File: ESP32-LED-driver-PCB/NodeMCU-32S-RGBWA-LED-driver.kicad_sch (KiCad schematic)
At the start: 24 parts, among them J1 PJ-037A, J2 TBP02R1-381-05BE, Q1 AO6404, Q2 AO6404, Q3 AO6404, Q4 AO6404, U1 NodeMCU-32S, U2 NCP1117-3.3_SOT223

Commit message: Re-organising folders
Re-organising folders
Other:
- note added: "5V to 12V, 5A input current maximum"
- note added: "For driving addressable LEDs: Remove resistors from R1-R4 and place them on R5-R7 Bridge JP1-JP3"
- note removed: "5V to 12V, 5A input power maximum"
- note removed: "For driving addressable LEDs: Remove resistors from R1-R4 and place them on R5-R7 Bridge JP1-JP3 Place 0R resistors R5-R7"
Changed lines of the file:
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@@
     (stroke (width 0) (type default) (color 0 0 0 0))
   )
-  (text "For driving addressable LEDs:\nRemove resistors from R1-R4 and place them on R5-R7\nBridge JP1-JP3\nPlace 0R resistors R5-R7\n"
+  (text "For driving addressable LEDs:\nRemove resistors from R1-R4 and place them on R5-R7\nBridge JP1-JP3"
     (at 137.16 52.07 0)
     (effects (font (size 1.27 1.27)) (justify left bottom))
   )
-  (text "5V to 12V, 5A input power maximum" (at 52.07 151.13 0)
+  (text "5V to 12V, 5A input current maximum" (at 52.07 151.13 0)
     (effects (font (size 1.27 1.27)) (justify left bottom))
   )

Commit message: Updated silkscreen
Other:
- note added: "For driving addressable LEDs: Remove 0R resistors from R1-R4 Place 0R resistors on R5-R7 Bridge JP1-JP3"
- note removed: "For driving addressable LEDs: Remove resistors from R1-R4 and place them on R5-R7 Bridge JP1-JP3"
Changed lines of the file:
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@@
     (stroke (width 0) (type default) (color 0 0 0 0))
   )
-  (text "For driving addressable LEDs:\nRemove resistors from R1-R4 and place them on R5-R7\nBridge JP1-JP3"
+  (text "For driving addressable LEDs:\nRemove 0R resistors from R1-R4\nPlace 0R resistors on R5-R7\nBridge JP1-JP3"
     (at 137.16 52.07 0)
     (effects (font (size 1.27 1.27)) (justify left bottom))

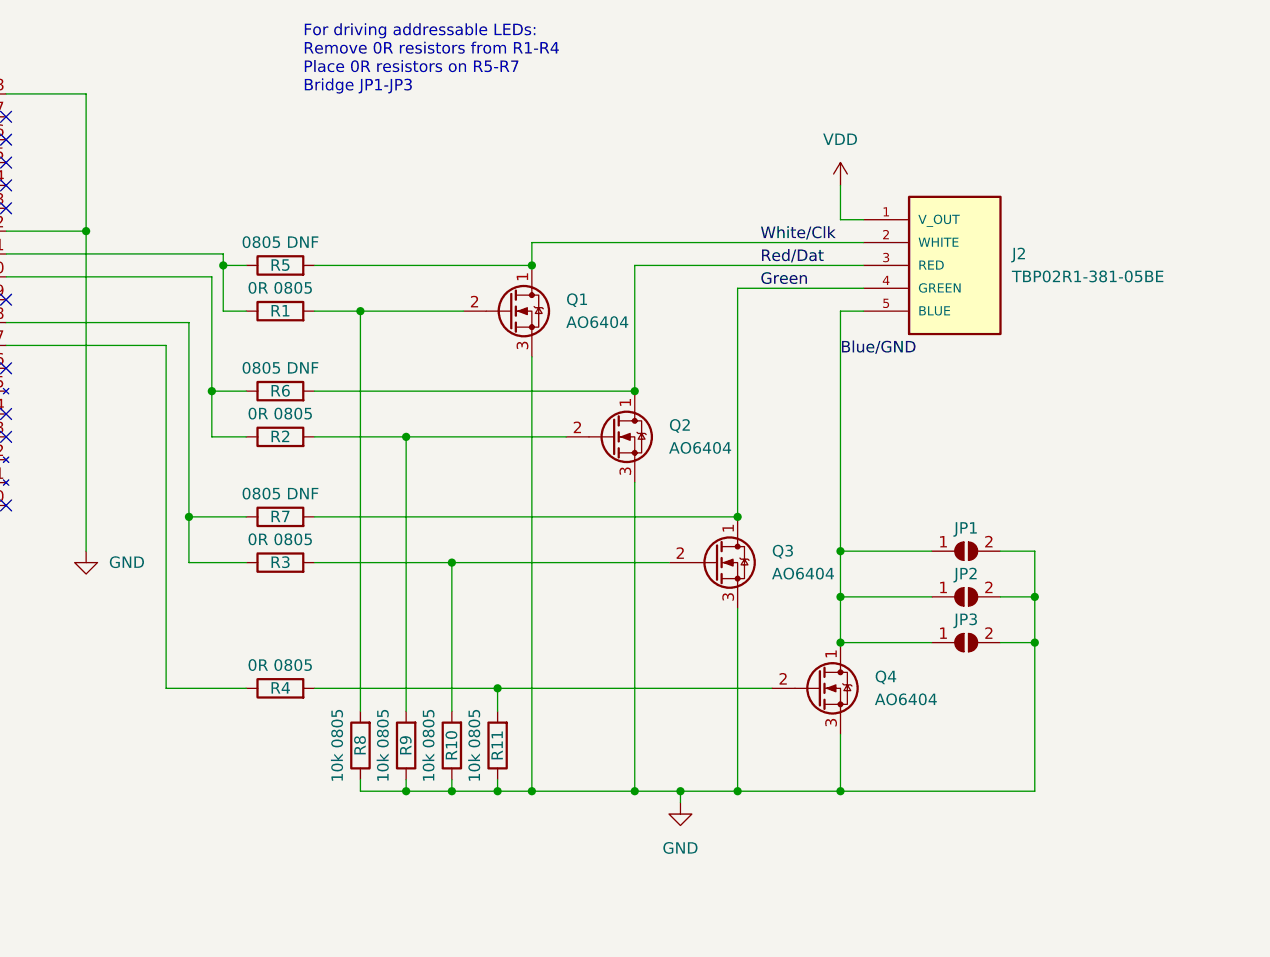
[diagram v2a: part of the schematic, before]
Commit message: Updated to 6 pin connector
Moved to 6 pin connector to get more addressable outputs with a dedicated ground pin.
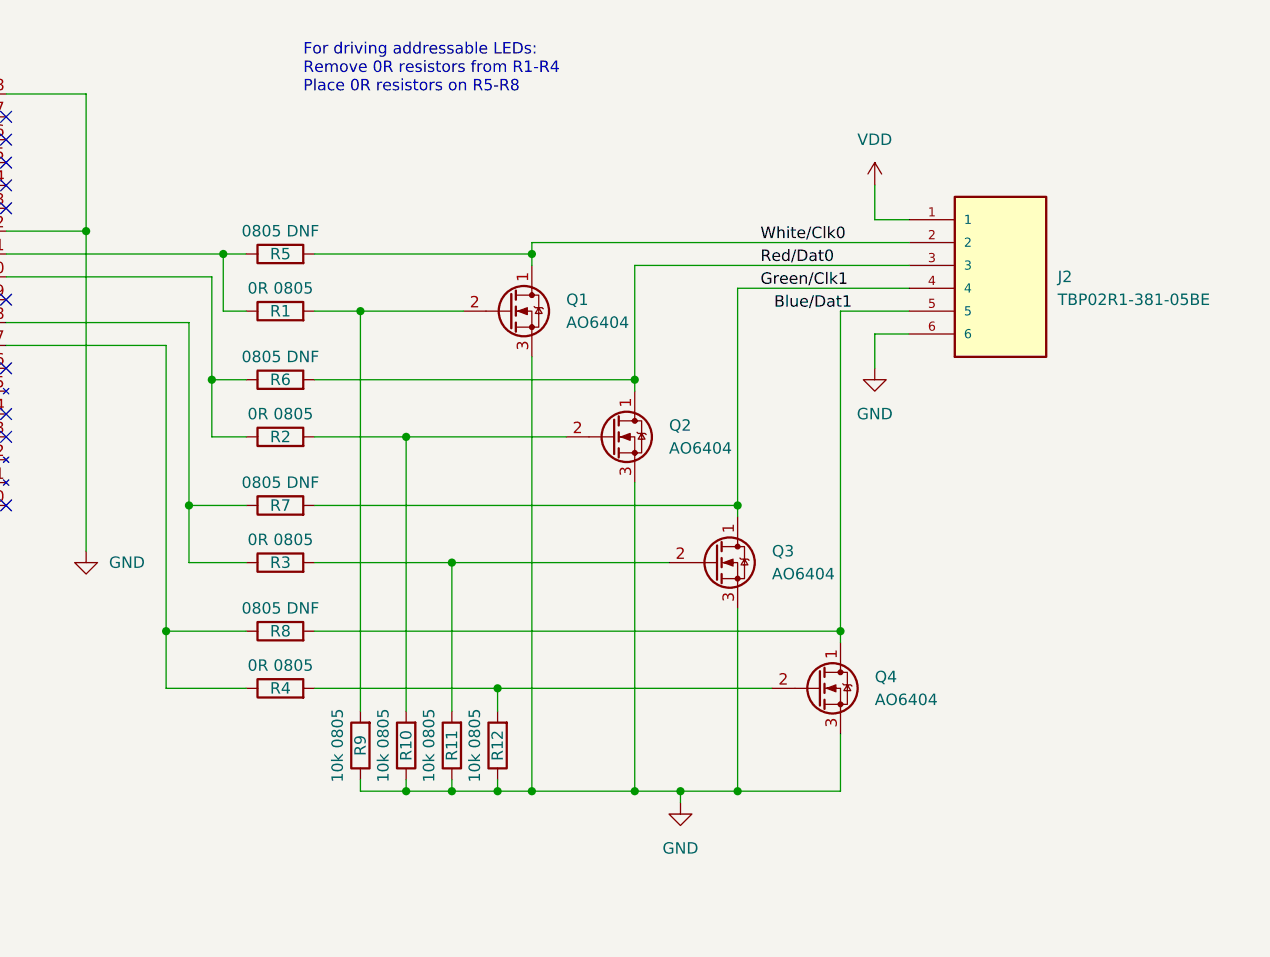
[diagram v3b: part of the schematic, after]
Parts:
- removed J2: TBP02R1-381-05BE, Matts_Library:CUI_TBP02R1-381-05BE, symbol Matts_Library:TBP02R1-381-05BE
- removed JP1, JP2, JP3: SolderJumper_2_Open, Jumper:SolderJumper-2_P1.3mm_Open_TrianglePad1.0x1.5mm, symbol Jumper:SolderJumper_2_Open
- added J2: TBP02R1-381-05BE, Matts_Library:CUI_TBP02R1-381-06BE, symbol Matts_Library:TBP02R1-381-06BE
- added R8: 0805 DNF, Resistor_SMD:R_0805_2012Metric, symbol Device:R
- renumbered R9 to R10, R10 to R11, R11 to R12, R8 to R9
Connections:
- net GND: now also J2.6
- net VDD: now also J2.1
- net at R4.1, U1.27 (IO16): now also R8.1
- net Blue/GND renamed Blue/Dat1
- net Blue/Dat1: now also J2.5, R8.2
- net Green renamed Green/Clk1
- net Green/Clk1: now also J2.4
- net Red/Dat renamed Red/Dat0
- net Red/Dat0: now also J2.3
- net White/Clk renamed White/Clk0
- net White/Clk0: now also J2.2
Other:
- note added: "For driving addressable LEDs: Remove 0R resistors from R1-R4 Place 0R resistors on R5-R8"
- note removed: "For driving addressable LEDs: Remove 0R resistors from R1-R4 Place 0R resistors on R5-R7 Bridge JP1-JP3"
- moved on the sheet: R5, R6, R7

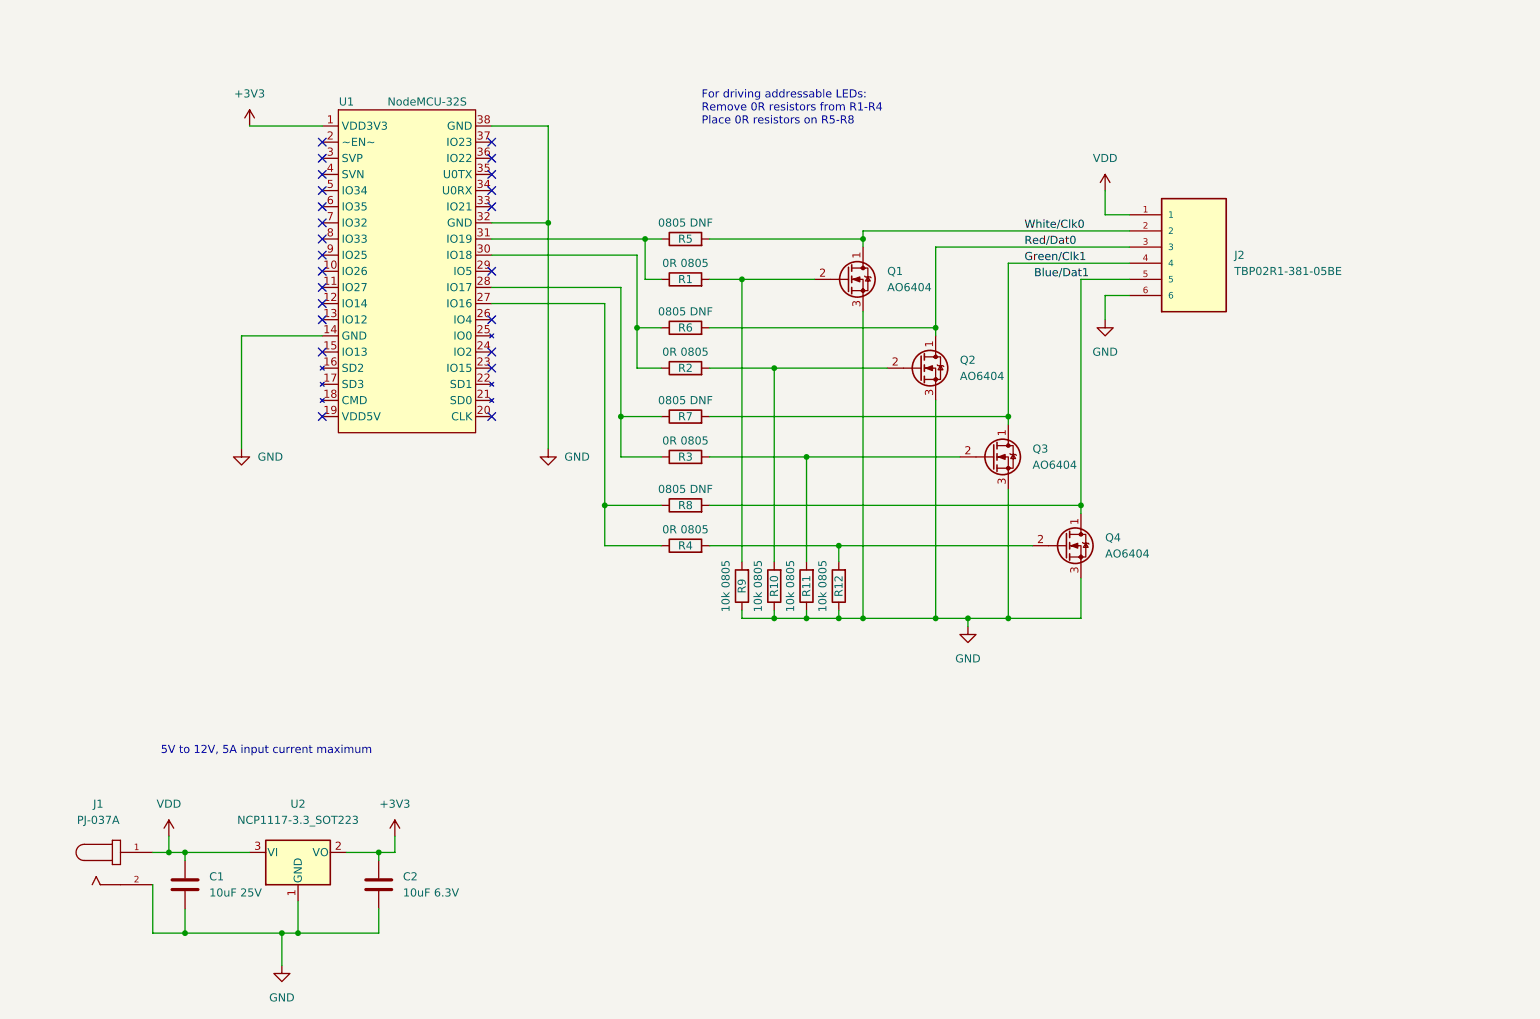
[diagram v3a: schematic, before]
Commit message: Added prototyping area
Added prototyping area to allow for extra sensors.
Updated some silkscreen
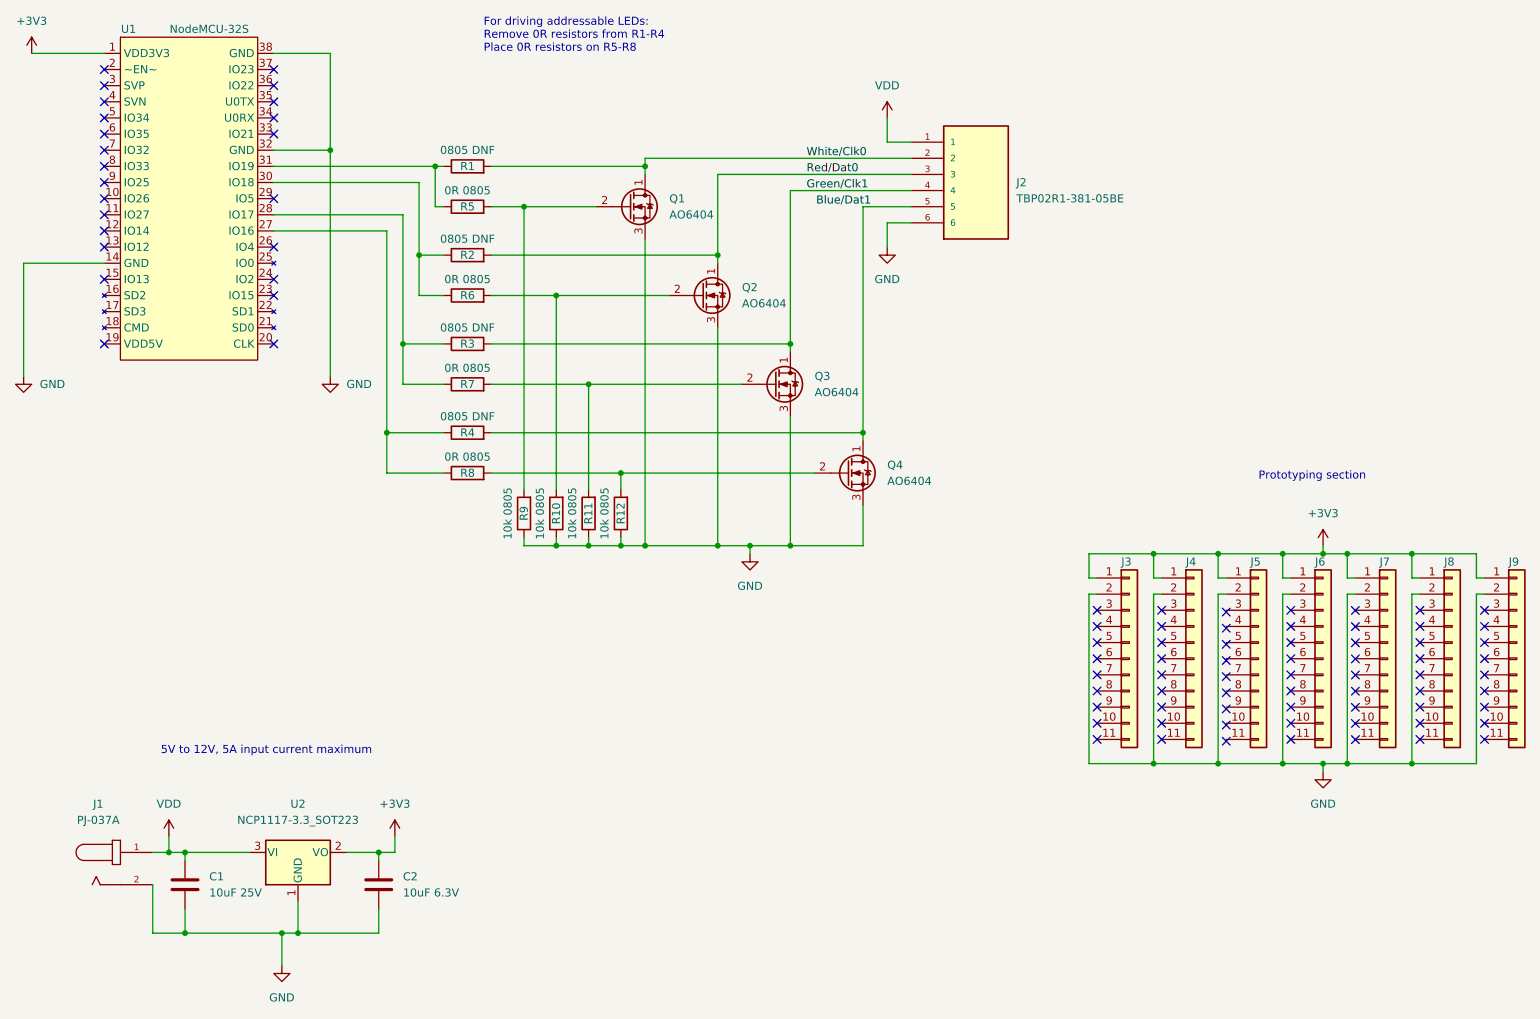
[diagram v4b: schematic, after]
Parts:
- added J3, J4, J5, J6, J7, J8, J9: Conn_01x11, Matts_Library:PinHeader_1x11_P2.54mm_Vertical, symbol Connector_Generic:Conn_01x11
- renumbered R5 to R1, R6 to R2, R7 to R3, R8 to R4, R1 to R5, R2 to R6, R3 to R7, R4 to R8
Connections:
- net +3V3: now also J3.1 (Pin_1), J4.1 (Pin_1), J5.1 (Pin_1), J6.1 (Pin_1), J7.1 (Pin_1), J8.1 (Pin_1), J9.1 (Pin_1)
- net GND: now also J3.2 (Pin_2), J4.2 (Pin_2), J5.2 (Pin_2), J6.2 (Pin_2), J7.2 (Pin_2), J8.2 (Pin_2), J9.2 (Pin_2)
- no-connect marks 24 -> 87
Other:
- note added: "Prototyping section"
- moved on the sheet: J2, Q1, Q2, Q3, Q4, R1, R10, R11, R12, R2, R3, R4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
